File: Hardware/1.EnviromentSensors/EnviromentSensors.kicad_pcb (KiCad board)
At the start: 2 copper layers, 14 parts, among them J2 Conn_01x05_Pin, U1 SHT4x, U2 BME680, U3 LPS22HB

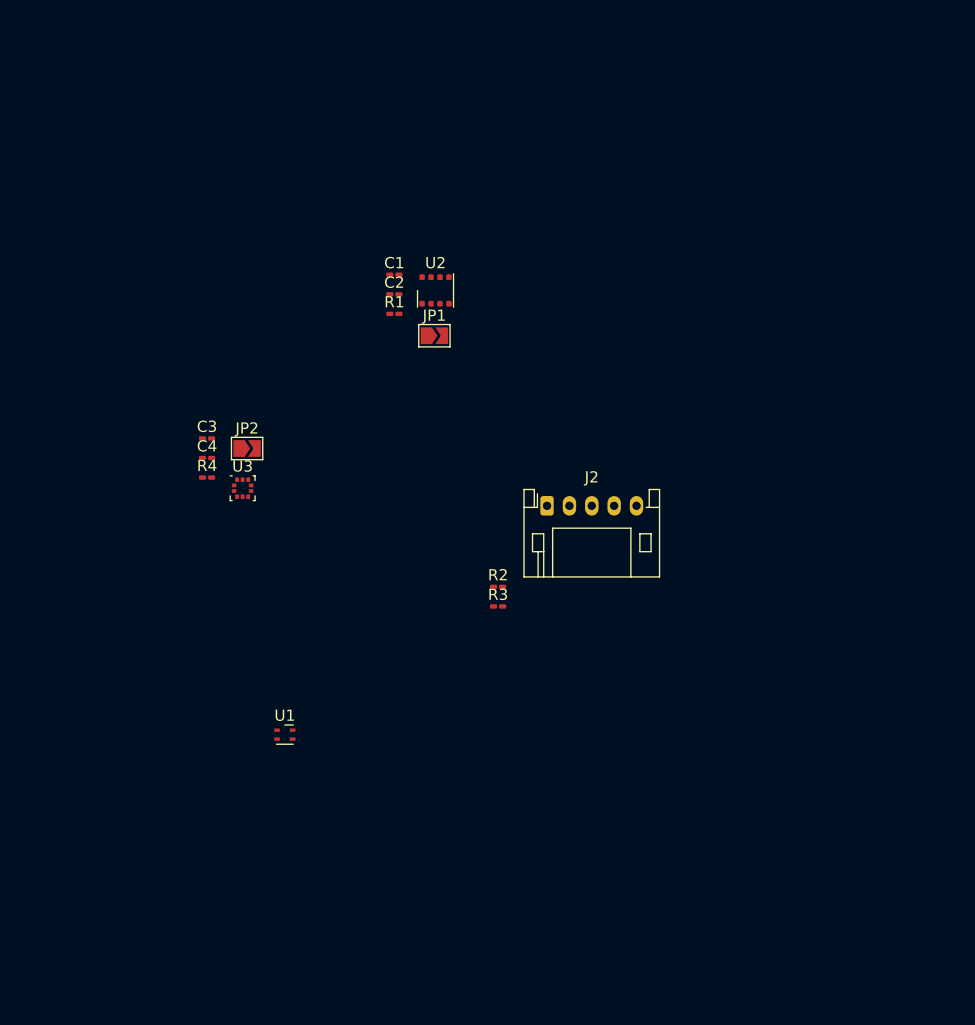
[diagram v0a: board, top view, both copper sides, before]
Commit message: Add initial version of Enviromental Sensors PCB
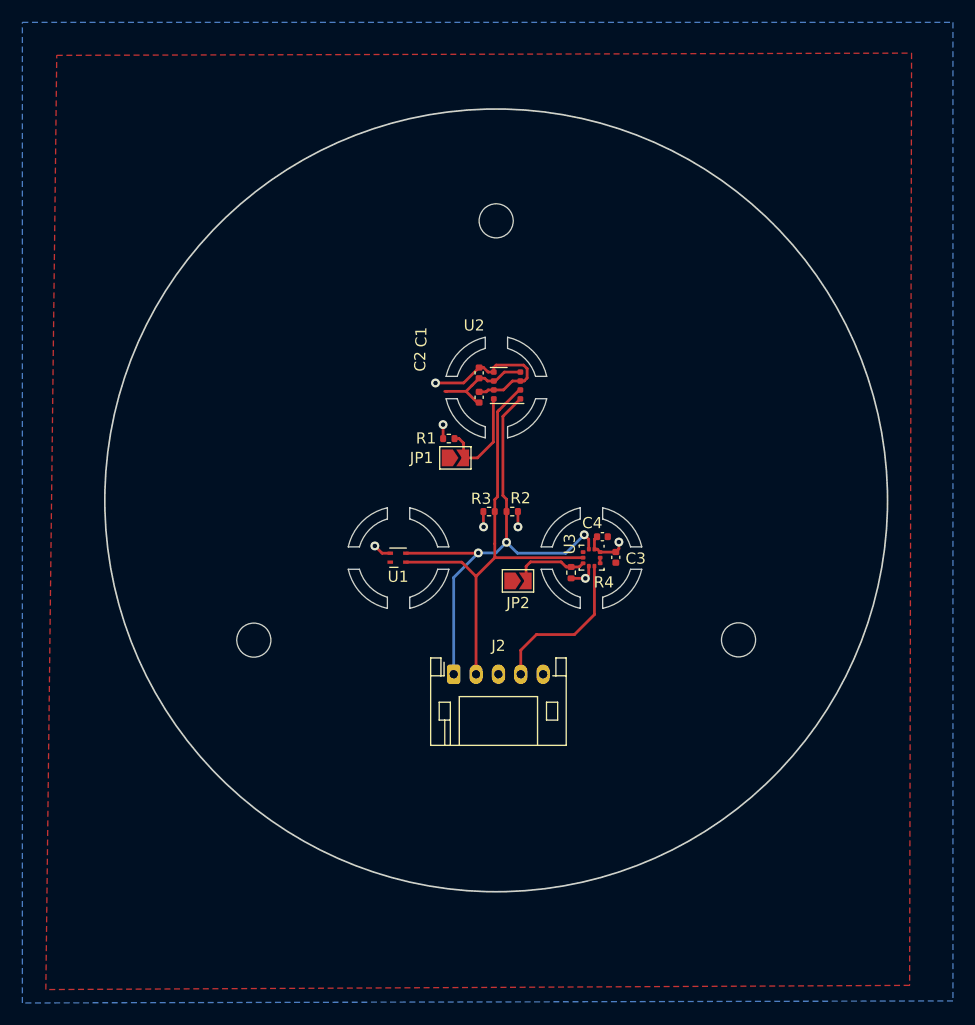
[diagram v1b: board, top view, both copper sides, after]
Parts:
- C1, C2, C3, C4: footprint Capacitor_SMD:C_0201_0603Metric_Pad0.64x0.40mm_HandSolder -> Capacitor_SMD:C_0402_1005Metric
- R1, R2, R3, R4: footprint Resistor_SMD:R_0201_0603Metric_Pad0.64x0.40mm_HandSolder -> Resistor_SMD:R_0402_1005Metric
- moved C3 38.1 mm to (145.7, 90.1), turned to -90 degrees
- moved C4 36.0 mm to (144.5, 88.2)
- moved R4 33.6 mm to (141.7, 91.5), turned to 90 degrees
- moved U3 31.8 mm to (143.5, 90.1), turned to -90 degrees
- moved JP2 27.0 mm to (136.9, 92.2)
- moved U1 18.8 mm to (126.2, 90.1), turned to 180 degrees
- moved J2 17.2 mm to (131.2, 100.5)
- moved R1 12.2 mm to (130.8, 79.5)
- moved C2 11.9 mm to (133.5, 75.8), turned to -90 degrees
- moved C1 11.6 mm to (133.5, 73.6), turned to -90 degrees
- moved JP1 11.1 mm to (131.3, 81.2)
- moved U2 10.6 mm to (136.0, 74.7), turned to -90 degrees
- moved R3 8.53 mm to (134.4, 86.0), turned to 180 degrees
- moved R2 6.86 mm to (136.4, 86.0), turned to 180 degrees
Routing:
- net I2C_SCL: track 0.00 -> 44.2 mm, vias 0 -> 3
- net I2C_SDA: track 0.00 -> 41.8 mm
- net +3.3V: track 0.00 -> 27.6 mm, vias 0 -> 7
- net LPS22HB_INT: track 0.00 -> 14.4 mm
- net GND: track 0.00 -> 9.77 mm
- net Net-(JP1-B): track 0.00 -> 9.37 mm
- net Net-(JP2-B): track 0.00 -> 6.88 mm
- added copper zone on B.Cu, net +3.3V
- added copper zone on F.Cu, net GND
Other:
- board outline added: 70 x 70 mm
